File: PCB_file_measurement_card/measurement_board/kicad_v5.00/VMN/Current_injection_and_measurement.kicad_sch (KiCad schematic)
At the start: 14 parts, among them J10 A/B, J11 Alim DPH5005, J12 Conn_01x08_Female, J13 Conn_01x02_Female, J14 Conn_01x02_Female, J15 Conn_01x08_Female, K3 AQY212EH, K4 AQY212EH, K5 AQY212EH, K6 AQY212EH, U5 1085-Adress=0X49

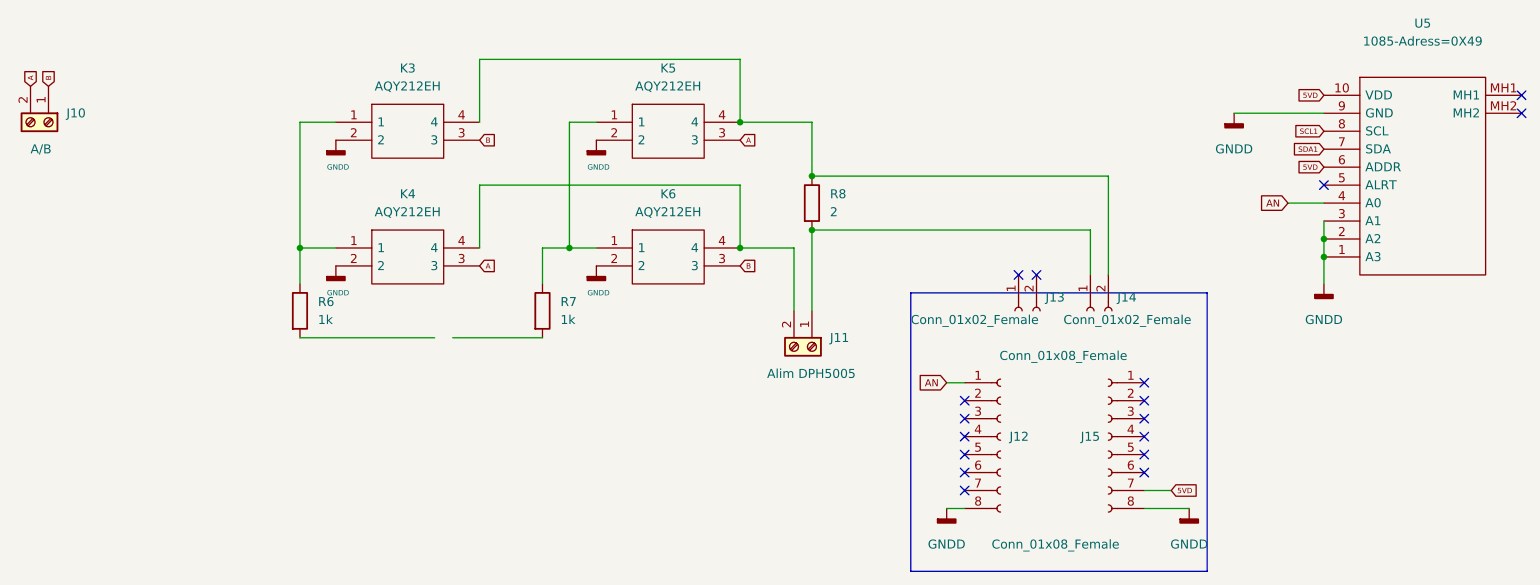
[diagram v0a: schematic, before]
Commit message: new schematics for V5.00
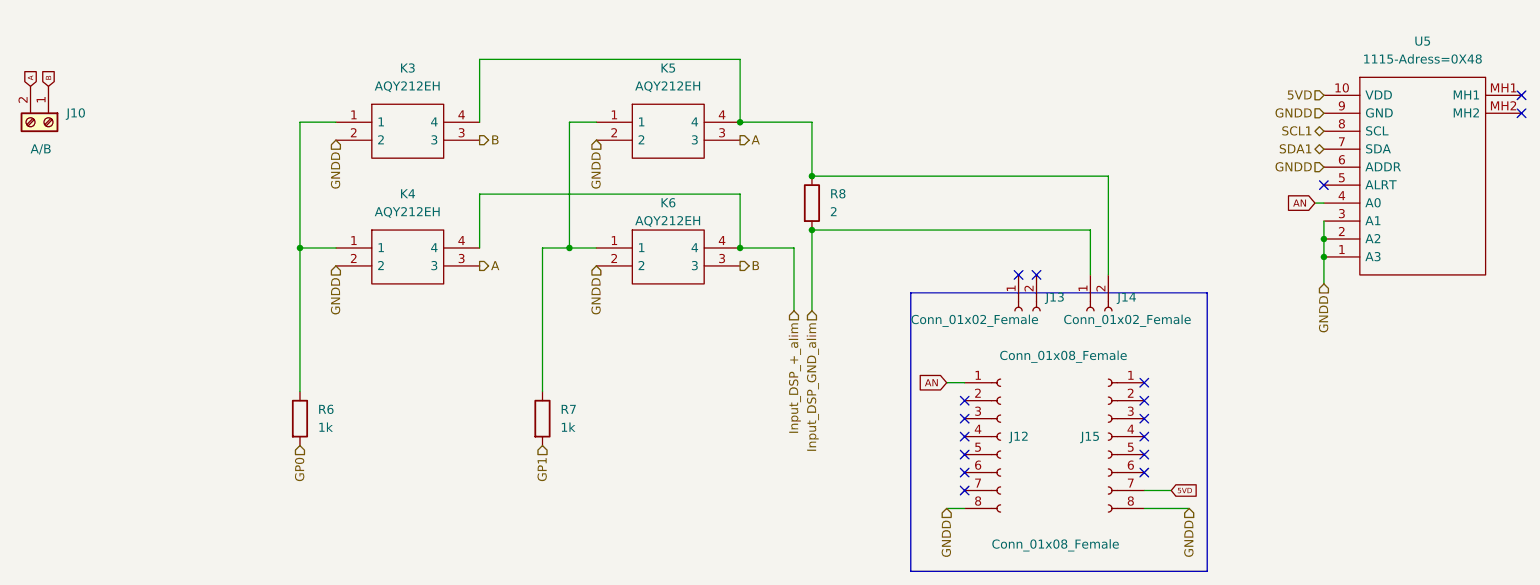
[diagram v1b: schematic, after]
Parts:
- removed J11: Alim DPH5005, TerminalBlock_Phoenix:TerminalBlock_Phoenix_MKDS-1,5-2-5.08_1x02_P5.08mm_Horizontal, symbol Connector:Screw_Terminal_01x02
- U5: value 1085-Adress=0X49 -> 1115-Adress=0X48
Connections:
- net 5VD: no longer U5.6 (ADDR)
- net GNDD: now also U5.6 (ADDR)
- net Input_DSP_+_alim: now reaches K4.4, K6.4
- net GP1: now reaches R7.2
- net Input_DSP_GND_alim: now reaches J14.1 (Pin_1), R8.2
- net GP0: now reaches R6.2
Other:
- moved on the sheet: R6, R7

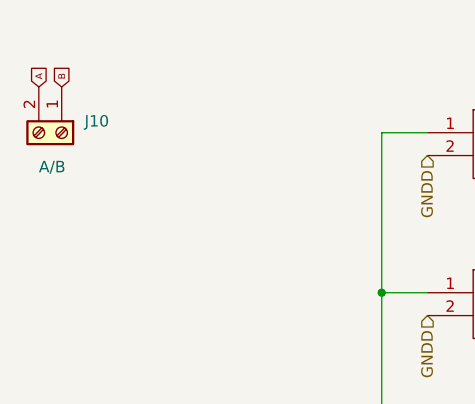
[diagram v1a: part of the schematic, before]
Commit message: new measurement board
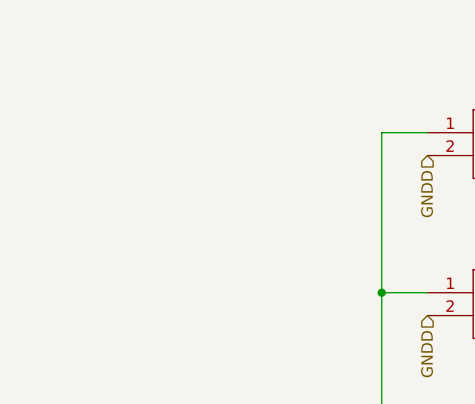
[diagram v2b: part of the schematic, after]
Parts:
- removed J10: A/B, TerminalBlock_Phoenix:TerminalBlock_Phoenix_MKDS-1,5-2-5.08_1x02_P5.08mm_Horizontal, symbol Connector:Screw_Terminal_01x02
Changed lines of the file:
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@@
     (stroke (width 0) (type default) (color 0 0 0 0))
-  )
-  (global_label "A" (shape input) (at 30.48 50.8 90) (fields_autoplaced)
-    (effects (font (size 0.75 0.75)) (justify left))
-    (property "Intersheet References" "${INTERSHEET_REFS}" (id 0) (at 30.4331 48.732 90)
-      (effects (font (size 0.75 0.75)) (justify left) hide)
-    )
   )
   (global_label "5VD" (shape input) (at 191.77 107.95 0) (fields_autoplaced)
@@
     (property "Intersheet References" "${INTERSHEET_REFS}" (id 0) (at 156.2152 92.6475 0)
       (effects (font (size 1 1)) (justify right) hide)
-    )
-  )
-  (global_label "B" (shape input) (at 33.02 50.8 90) (fields_autoplaced)
-    (effects (font (size 0.75 0.75)) (justify left))
-    (property "Intersheet References" "${INTERSHEET_REFS}" (id 0) (at 32.9731 48.6249 90)
-      (effects (font (size 0.75 0.75)) (justify left) hide)
     )
   )
@@
     (pin "8")
   )
-  (symbol (lib_id "Connector:Screw_Terminal_01x02") (at 33.02 55.88 270) (unit 1)
-    (in_bom yes) (on_board yes)
-    (property "Reference" "J10" (id 0) (at 35.56 54.6099 90)
-      (effects (font (size 1.27 1.27)) (justify left))
-    )
-    (property "Value" "A/B" (id 1) (at 30.48 59.69 90)
-      (effects (font (size 1.27 1.27)) (justify left))
-    )
-    (property "Footprint" "TerminalBlock_Phoenix:TerminalBlock_Phoenix_MKDS-1,5-2-5.08_1x02_P5.08mm_Horizontal" (id 2) (at 33.02 55.88 0)
-      (effects (font (size 1.27 1.27)) hide)
-    )
-    (property "Datasheet" "~" (id 3) (at 33.02 55.88 0)
-      (effects (font (size 1.27 1.27)) hide)
-    )
-    (pin "1")
-    (pin "2")
-  )
   (symbol (lib_id "Device:R") (at 68.58 97.79 0) (unit 1)

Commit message: last version of measurement board, with op07
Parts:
- removed J13: Conn_01x02_Female, Connector_PinHeader_2.54mm:PinHeader_1x02_P2.54mm_Vertical, symbol Connector:Conn_01x02_Female
- added J20: shunt +, Connector_PinHeader_2.54mm:PinHeader_1x01_P2.54mm_Vertical, symbol Connector_Generic:Conn_01x01
- added J21: shunt -, Connector_PinHeader_2.54mm:PinHeader_1x01_P2.54mm_Vertical, symbol Connector_Generic:Conn_01x01
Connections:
- net Input_DSP_GND_alim: now also J21.1 (Pin_1)
- net at J14.2 (Pin_2), K3.4, K5.4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: now also J20.1 (Pin_1)
- no-connect marks 17 -> 15
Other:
- moved on the sheet: K3, K4, K5, K6, R6, R7, R8
